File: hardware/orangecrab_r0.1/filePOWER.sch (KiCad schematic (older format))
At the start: 46 parts, among them J5 JST, U1 FAN53541, U10 NCP167, U2 FAN53541, U5 BQ24230, U7 FAN53541, U8 TPS51206

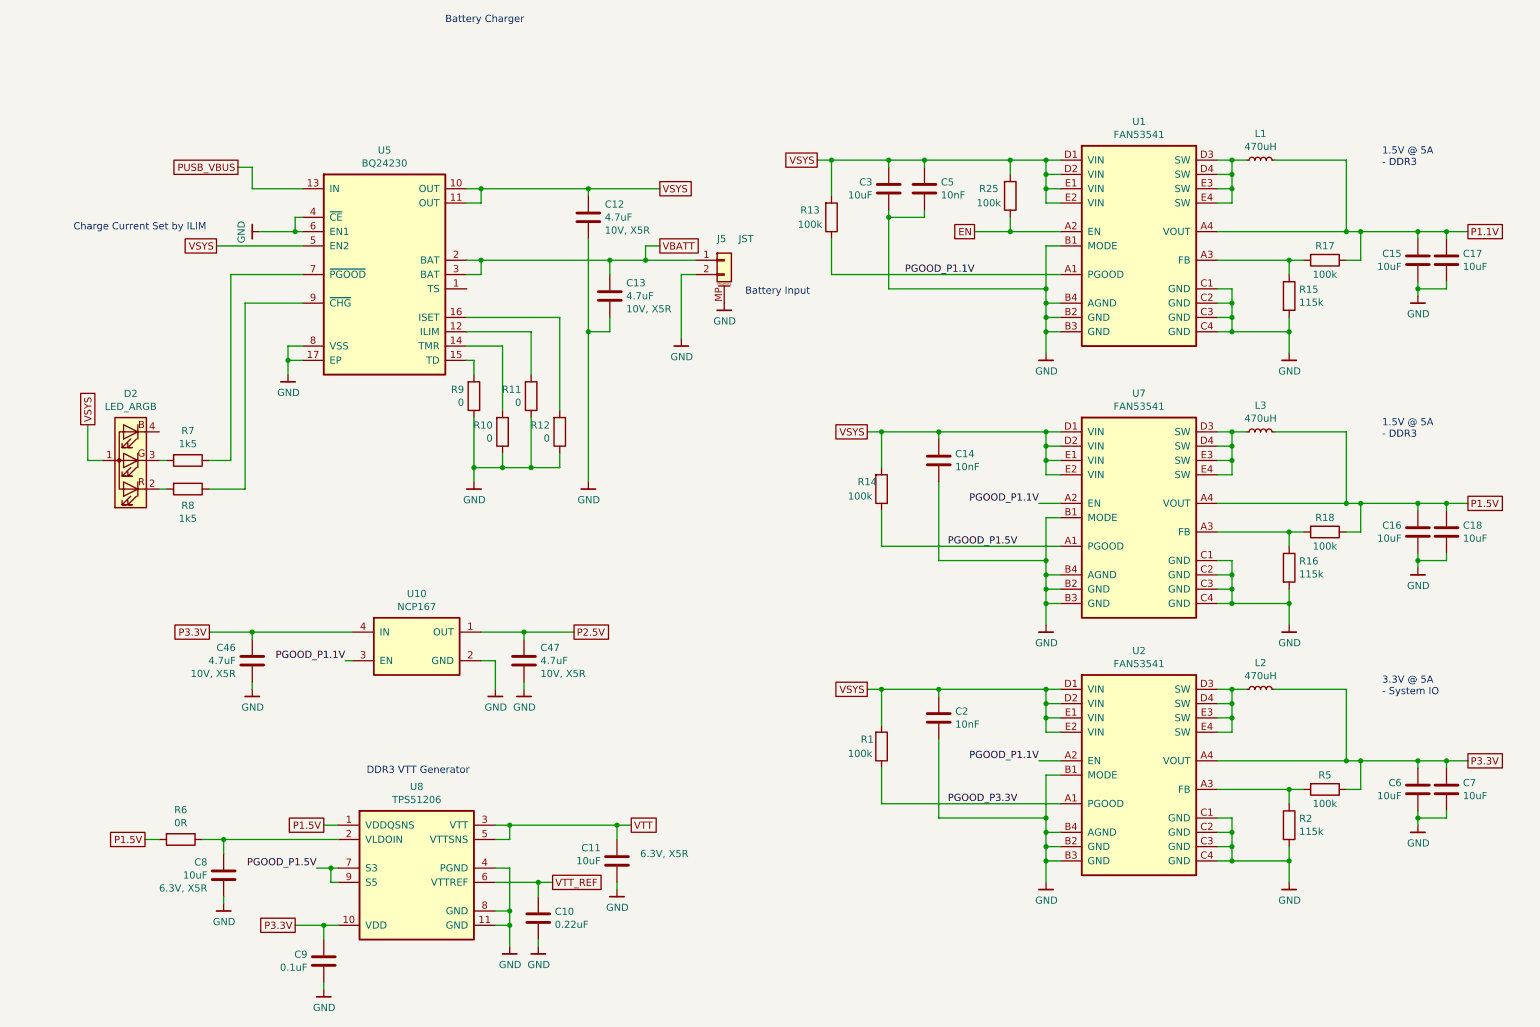
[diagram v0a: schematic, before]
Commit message: Added pulldown on TS pin to disable TS func. Added 4.7uF cap to USB input. Corrected Battery polarity Calculated correct DCDC Fb Added pullup to SWCLK Added Pulldown to TCK Added Pinout legend on top layer Fixed Missing VCC on Flash Neaten up Power Plane Schematic Checklist complete.
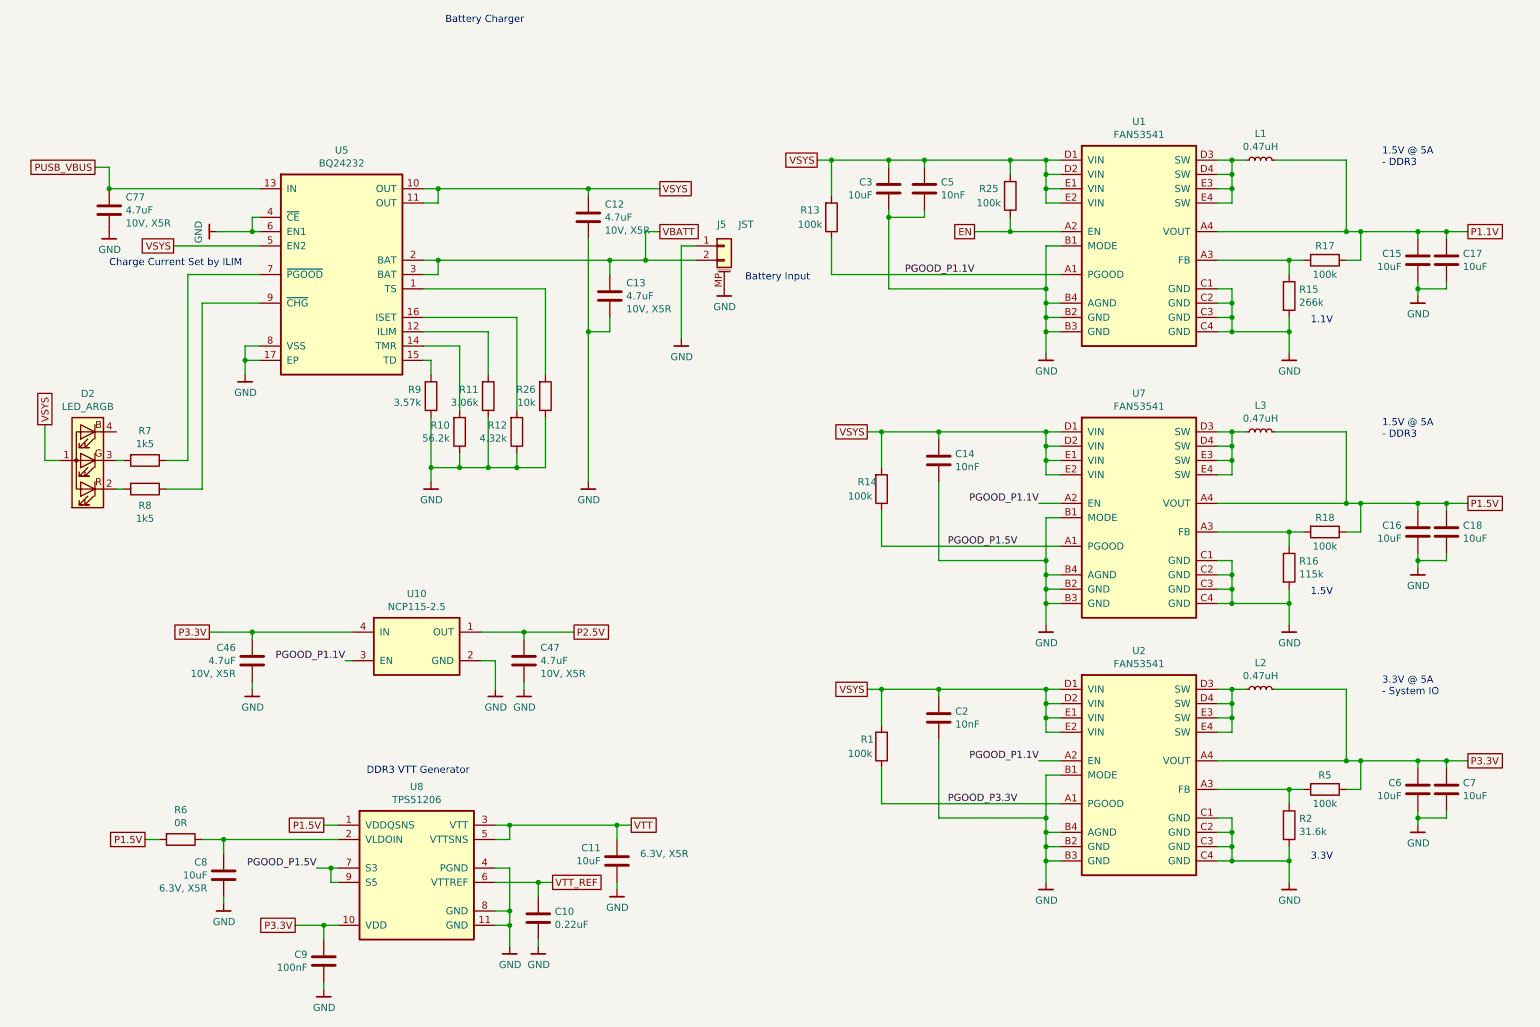
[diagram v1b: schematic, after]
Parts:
- added C77: 4.7uF, Capacitor_SMD:C_0402_1005Metric, symbol Device:C
- added R26: 10k, Resistor_SMD:R_0201_0603Metric, symbol Device:R
- C9: value 0.1uF -> 100nF
- J5: PN (none) -> S2B-PH-SM4-TB(LF)(SN)
- L1, L2, L3: value 470uH -> 0.47uH
- R10: value 0 -> 56.2k
- R11: value 0 -> 3.06k
- R12: value 0 -> 4.32k
- R15: value 115k -> 266k
- R2: value 115k -> 31.6k
- R9: value 0 -> 3.57k
- U1, U2, U7: PN (none) -> FAN53541UCX
- U10: value NCP167 -> NCP115-2.5; PN (none) -> NCP115CMX250TCG
- U5: value BQ24230 -> BQ24232
- U8: PN (none) -> TPS51206DSQR
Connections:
- net GND: now also J5.1 (Pin_1), C77.2, R26.1; no longer J5.2 (Pin_2)
- net PUSB_VBUS: now also C77.1
- net VBATT: now also J5.2 (Pin_2); no longer J5.1 (Pin_1)
- net at U5.1 (TS): now also R26.2
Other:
- note added: "1.1V"
- note added: "1.5V"
- note added: "3.3V"
- moved on the sheet: D2, J5, R10, R11, R12, R7, R8, R9, U5

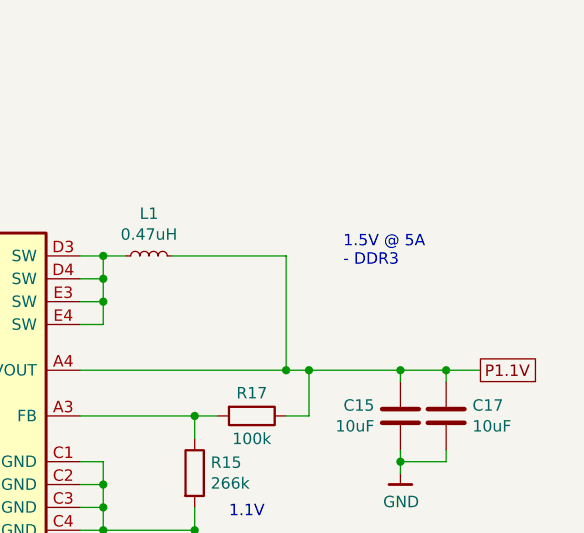
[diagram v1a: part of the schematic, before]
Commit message: Fix stale comment on PSU voltage/subsystem
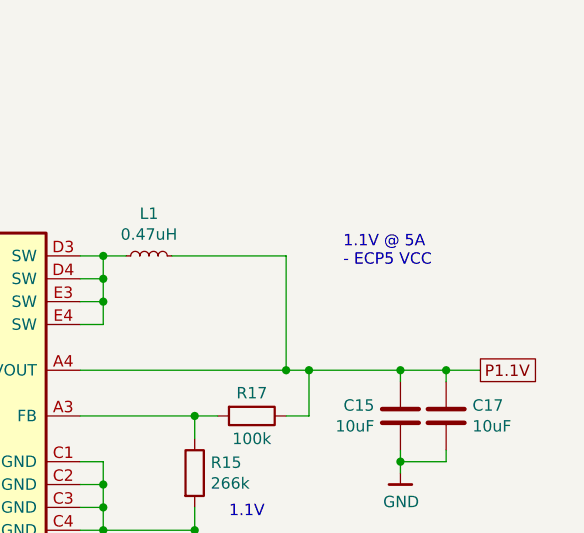
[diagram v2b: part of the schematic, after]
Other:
- note added: "1.1V @ 5A\n- ECP5 VCC\n"
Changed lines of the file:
@@
 $EndComp
 Text Notes 10100 1250 0    50   ~ 0
-1.5V @ 5A\n- DDR3\n
+1.1V @ 5A\n- ECP5 VCC\n
 Wire Wire Line
 	7850 1500 7750 1500

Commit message: Fixed TPS551206 regulator footprint 2x2 DFN10
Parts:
- U8: footprint Package_DFN_QFN:DFN-10-1EP_3x3mm_P0.5mm_EP1.7x2.5mm -> gkl_housings_dfn:WSON-10-1EP_2x2mm_P0.4mm
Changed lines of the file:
@@
 F 0 "U8" H 3350 6819 50  0000 C CNN
 F 1 "TPS51206" H 3350 6728 50  0000 C CNN
-F 2 "Package_DFN_QFN:DFN-10-1EP_3x3mm_P0.5mm_EP1.7x2.5mm" H 3350 6750 50  0001 C CNN
+F 2 "gkl_housings_dfn:WSON-10-1EP_2x2mm_P0.4mm" H 3350 6750 50  0001 C CNN
 F 3 "" H 3350 6750 50  0001 C CNN
 F 4 "TPS51206DSQR" H 3350 6200 50  0001 C CNN "PN"

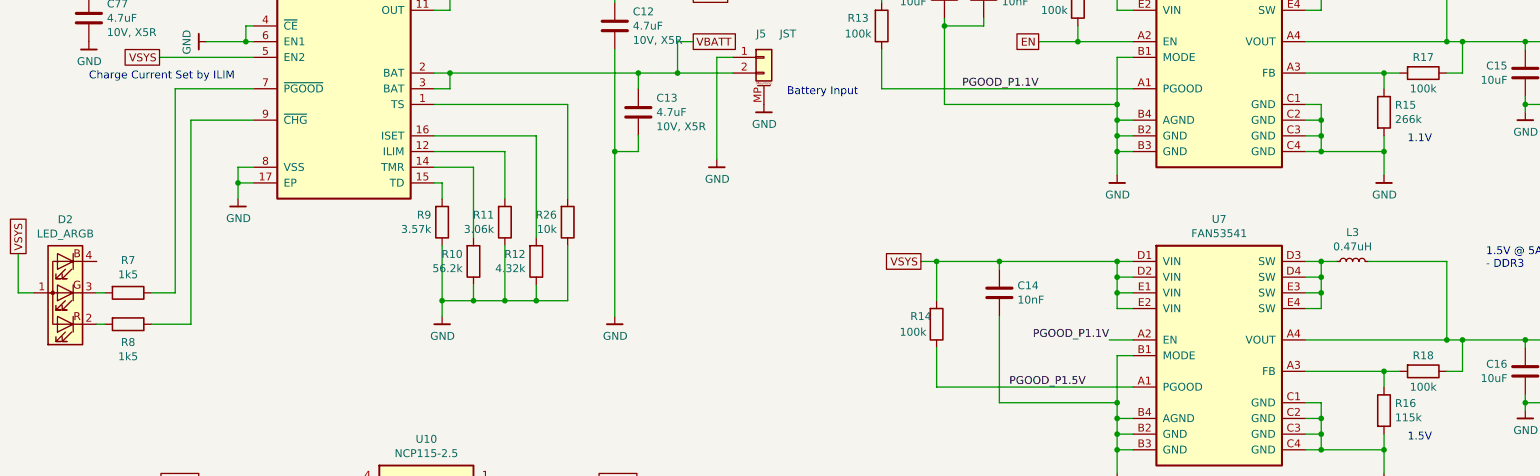
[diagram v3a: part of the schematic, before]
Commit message: Updated BOM fields in KiCad project Exported ibom Clarify fab notes
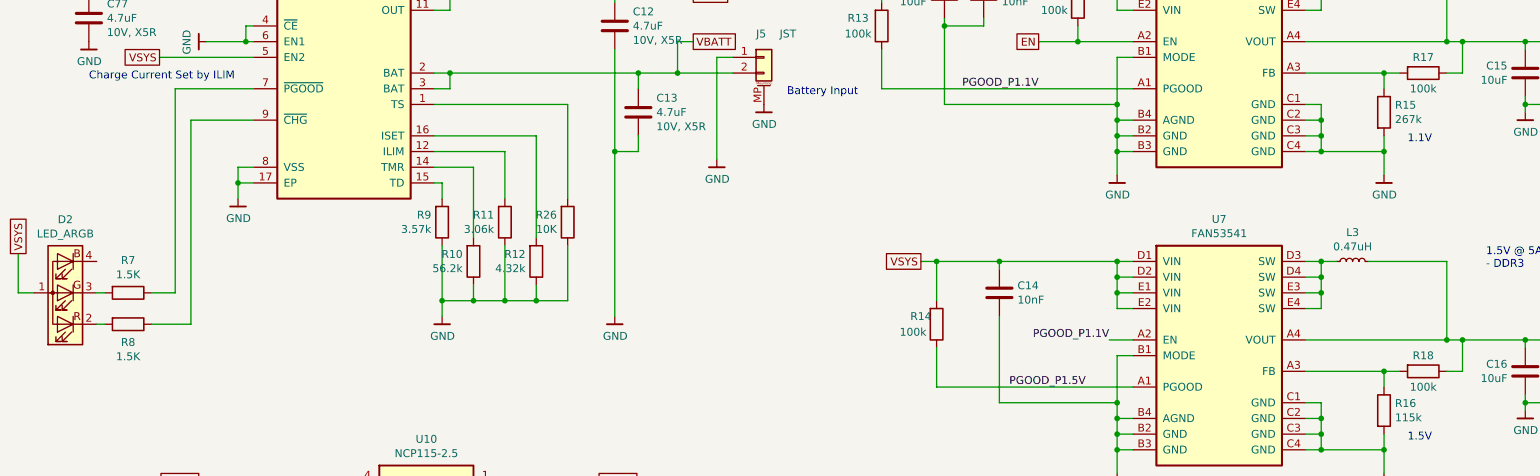
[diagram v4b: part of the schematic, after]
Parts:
- C10: Mfg (none) -> Samsung Electro-Mechanics; PN (none) -> CL03A224MQ3NNNC
- C11, C15, C16, C17, C18, C6, C7, C8: Mfg (none) -> Murata Electronics North America; PN (none) -> GRM155R60J106ME15D
- C12, C13, C46, C47, C77: Mfg (none) -> Murata Electronics North America; PN (none) -> GRM155R61A475MEAAD
- C14, C2, C5: Mfg (none) -> Samsung Electro-Mechanics; PN (none) -> CL03B103KP3NNNC
- C3: Mfg (none) -> Taiyo Yuden; PN (none) -> LMK107BBJ106MALT
- C9: Mfg (none) -> Samsung Electro-Mechanics; PN (none) -> CL03A104KQ3NNNC
- D2: Mfg (none) -> ‎Wurth Electronics Inc.‎; PN (none) -> 150044M155260
- J5: Mfg (none) -> JST Sales America Inc.
- L1, L2, L3: Mfg (none) -> Samsung Electro-Mechanics; PN (none) -> CIGT201210UHR47MNE
- R1, R13, R14, R17, R18, R25, R5: Mfg (none) -> ‎Yageo‎; PN (none) -> RC0201FR-07100KL
- R10: Mfg (none) -> ‎Yageo‎; PN (none) -> RC0201FR-0756K2L
- R11: Mfg (none) -> ‎Yageo‎; PN (none) -> RC0201FR-073K09L
- R12: Mfg (none) -> ‎Yageo‎; PN (none) -> RC0201FR-074K32L
- R15: value 266k -> 267k; Mfg (none) -> ‎Yageo‎; PN (none) -> RC0201FR-07267KL
- R16: Mfg (none) -> ‎Yageo‎; PN (none) -> RC0201FR-07115KL
- R2: Mfg (none) -> ‎Yageo‎; PN (none) -> RC0201FR-0731K6L
- R26: value 10k -> 10K; Mfg (none) -> ‎Yageo‎; PN (none) -> RC0201FR-0710KL
- R6: Mfg (none) -> ‎Yageo‎; PN (none) -> RC0402FR-070RL
- R7, R8: value 1k5 -> 1.5K; Mfg (none) -> ‎Yageo‎; PN (none) -> RC0201FR-071K5L
- R9: Mfg (none) -> ‎Yageo‎; PN (none) -> RC0201FR-073K57L
- U1, U10, U2, U7: Mfg (none) -> ON Semiconductor
- U8: Mfg (none) -> Texas Instruments
